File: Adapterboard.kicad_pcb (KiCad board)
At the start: 2 copper layers, 100 x 100 mm, 72 parts, among them J101 Conn_01x01_Pin, J102 Conn_01x01_Pin, J103 JTAG, J104 Conn_01x01_Pin, J105 TUNNEL_IN, J106 +15V in, J107 -15V in, J108 Power to Preamp, J109 Piezo, J110 2xPin, J111 5xPin, U102 DAC X, U103 ESP32-DEVKITC-32D, U104 DAC Y, U106 DAC Z, U107 ADC 8 Click, U108 mint, U109 UniRegensburg, U110 OTH, U201 TL072, U301 TL072

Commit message: complete for production
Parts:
- D103: value LED_RED -> RED
- D109: value LED -> LED_+15V
- D110: value LED -> LED_-15V
- J101, J102, J104: value Conn_01x01_Pin -> 1xPin; footprint Connector_PinHeader_1.00mm:PinHeader_1x01_P1.00mm_Vertical -> Connector_PinHeader_2.54mm:PinHeader_1x01_P2.54mm_Vertical
- J106: value +15V in -> Power in +15V
- J107: value -15V in -> Power in -15V
- J108: value Power to Preamp -> Power out Preamplifier
- J110: value 2xPin -> TUNNEL_1
- J111: value 5xPin -> USB_Connector
- R302: value K3 -> 3K3
- moved J105 0.37 mm to (137.2, 57.3)
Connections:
- J105 pad 1: /TUNNEL_IN -> /TUNNEL_GND
- J105 pad 2: /TUNNEL_GND -> /TUNNEL_IN
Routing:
- net GND: track 0.00 -> 11.9 mm
- net Z: track 82.3 -> 84.0 mm
- net /TUNNEL_GND: track 33.8 -> 32.9 mm
- net /TUNNEL_IN: track 17.4 -> 16.7 mm
- net Net-(C205-Pad1): track 47.7 -> 48.5 mm
- net ESP32_SDO: track 121.1 -> 120.4 mm
- added copper zone on B.Cu, net GND
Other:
- board text added: "+15V"
- board text added: "-15V"
- board text added: "2*Pin"
- board text added: "5xPin"
- board text added: "PIEZO"
- board text added: "RxD<-"
- board text added: "TUNNEL VCC"
- board text added: "TxD->"
- board text removed: "+15V in"
- board text removed: "-15V in"
- board text removed: "PIEZO out"
- board text removed: "RxD"
- board text removed: "TUNNEL VCC out"
- board text removed: "TxD"

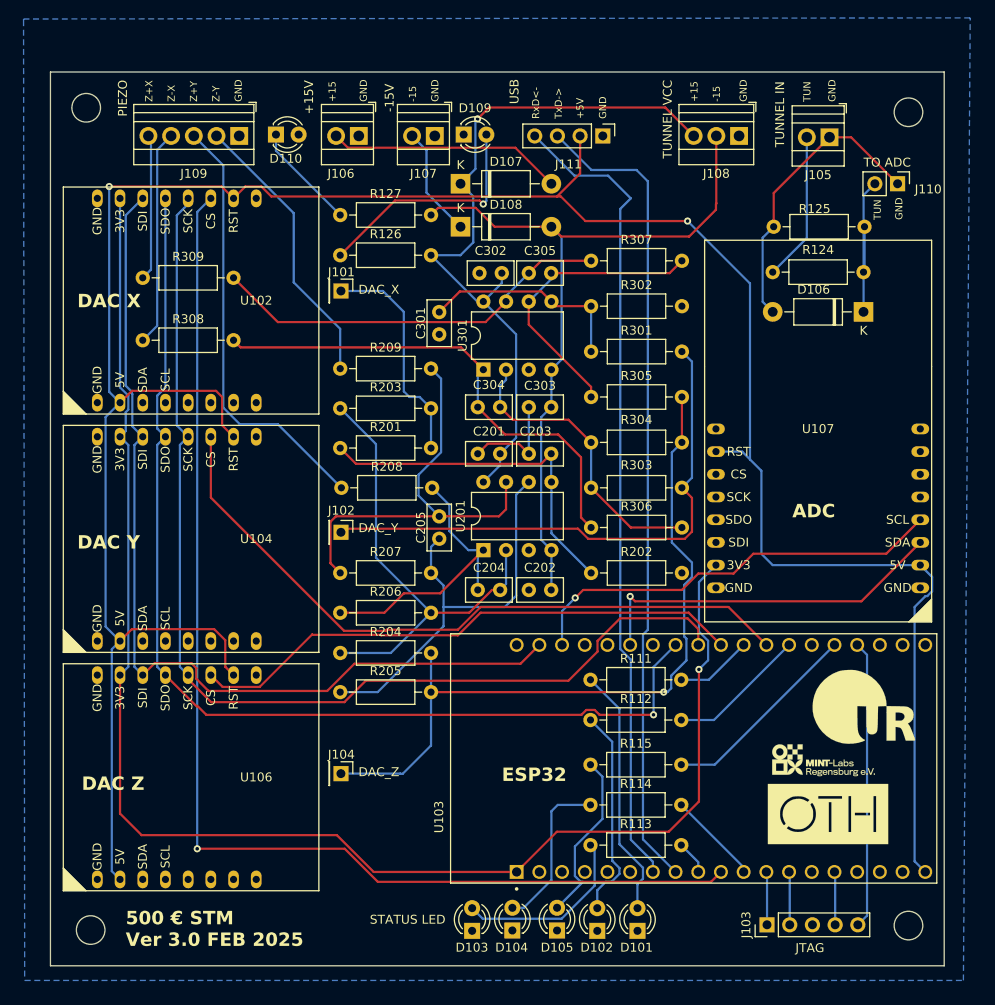
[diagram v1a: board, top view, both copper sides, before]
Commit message: ADS1115 added
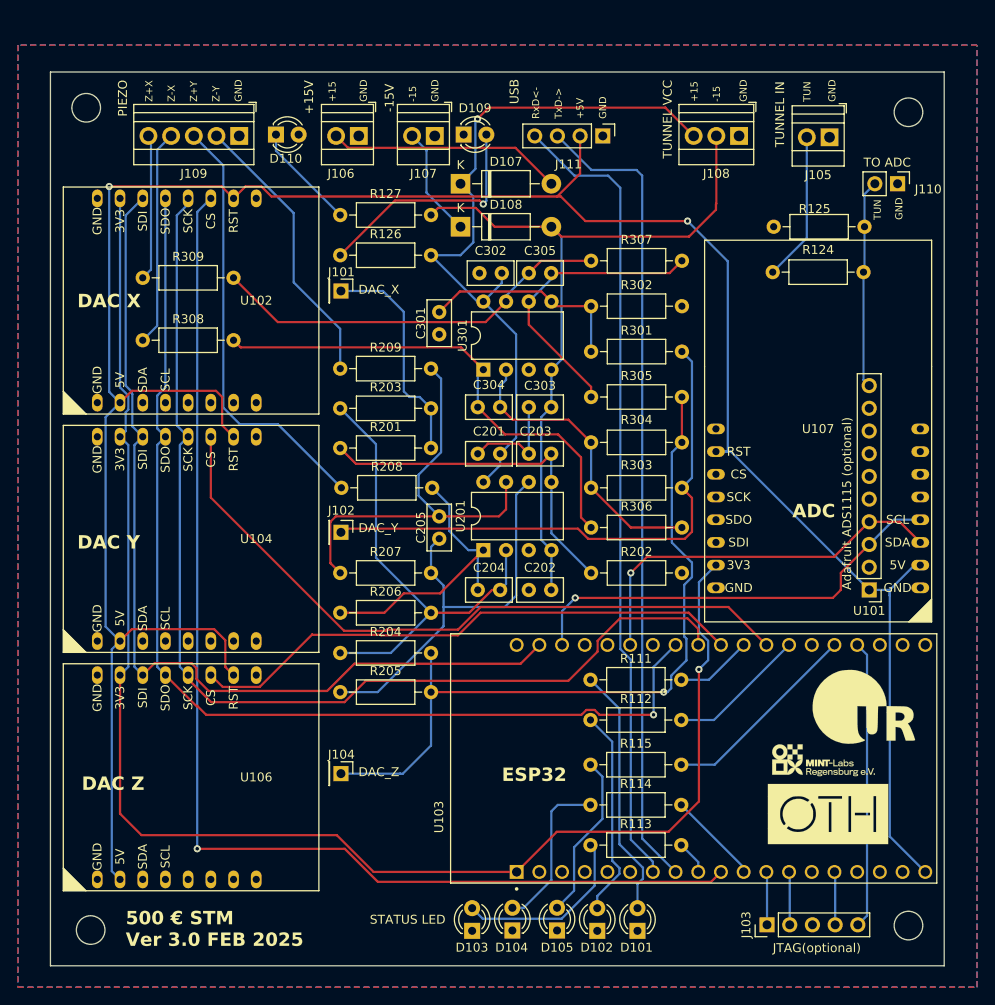
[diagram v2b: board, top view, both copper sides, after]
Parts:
- removed D106: 1N5819, Diode_THT:D_DO-41_SOD81_P10.16mm_Horizontal
- added U101: ADS1115A, Connector_PinHeader_2.54mm:PinHeader_1x10_P2.54mm_Vertical, F.Cu at (141.6, 107.9)
- D103: value RED -> LED_RED
- D104: value YELLOW -> LED_YELLOW
- D105: value GREEN -> LED_GREEN
- J101, J102, J104: value 1xPin -> Conn_01x01_Pin
- R302: value 3K3 -> K3
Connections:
- net /TUNNEL_TO_ADC_A3 renamed TUNNEL_TO_ADC_A3
- J105 pad 1: /TUNNEL_GND -> GND
- J110 pad 1: /TUNNEL_GND -> GND
- R125 pad 2: /TUNNEL_GND -> GND
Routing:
- net /TUNNEL_GND: track 32.9 -> 0.00 mm
- net +5V: track 289.2 -> 283.0 mm
- net TUNNEL_TO_ADC_A3: track 20.0 -> 23.5 mm
- net ESP32_SDA: track 41.0 -> 43.8 mm
- net ESP32_SCL: track 48.1 -> 49.2 mm
- net RXD: track 91.0 -> 90.0 mm
- net /LED_GREEN: track 19.6 -> 18.7 mm
- added copper zone on F.Cu, net GND
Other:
- board text added: "Adafruit ADS1115 (optional)"
- board text added: "JTAG(optional)"
- board text removed: "JTAG"
